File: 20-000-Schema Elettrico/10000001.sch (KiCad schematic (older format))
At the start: 1 part

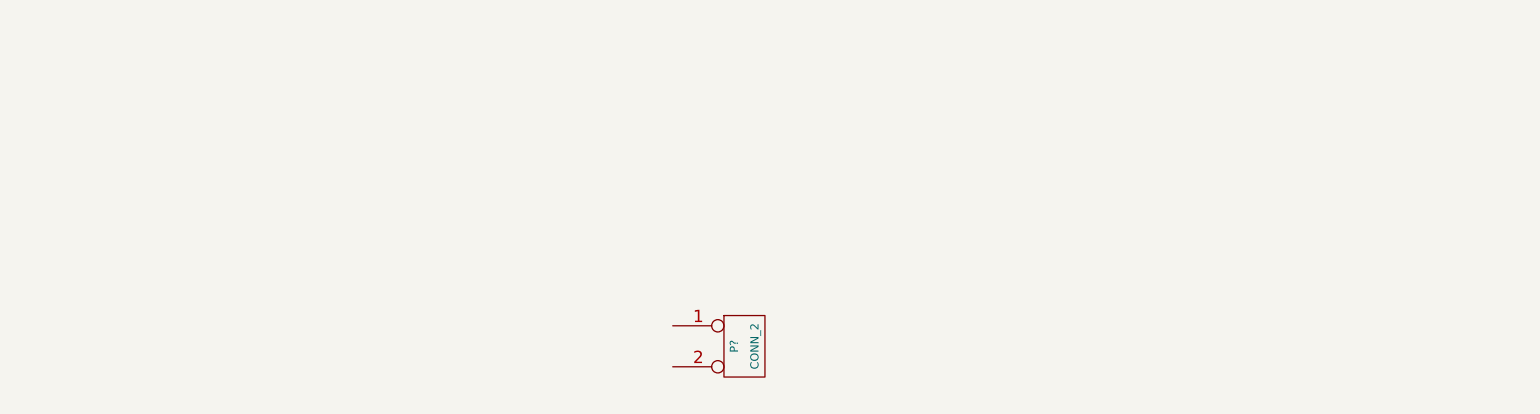
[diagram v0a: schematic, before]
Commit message: Aggiunti documenti di descrizione interfacce RS232, USB e distribuzione alimentazione... manca solo ADC!
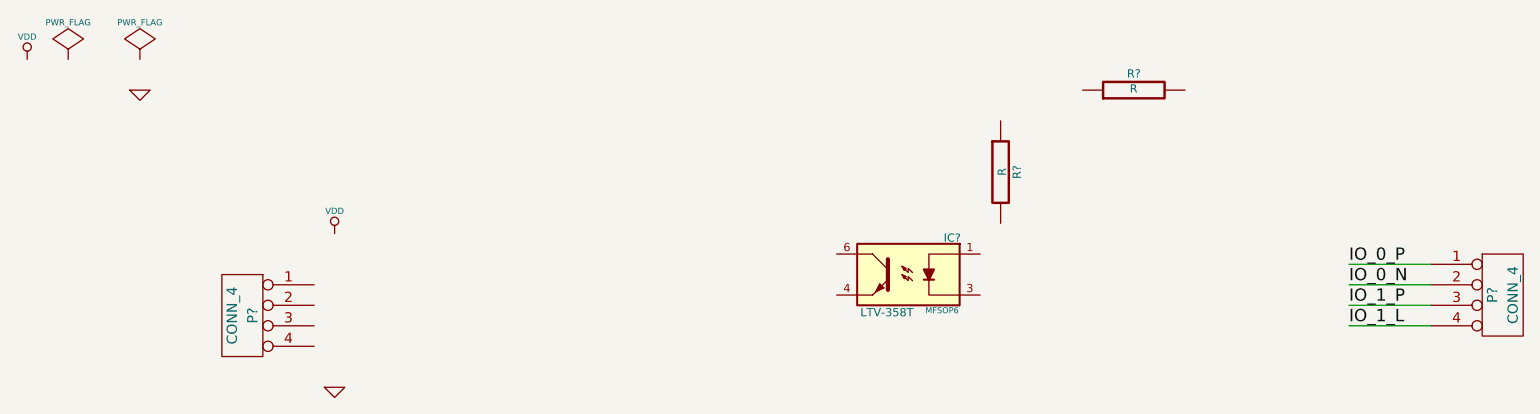
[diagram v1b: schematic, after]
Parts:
- removed P?: CONN_2, symbol CONN_2
- added IC?: LTV-358T, MFSOP6, symbol LTV-358T
- added P? (x2): CONN_4, symbol CONN_4
- added R? (x2): R, ~, symbol R
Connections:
- new net IO_0_N: P?.2 (P2)
- new net IO_0_P: P?.1 (P1)
- new net IO_1_L: P?.4 (P4)
- new net IO_1_P: P?.3 (P3)
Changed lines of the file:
@@
 Sheet 1 1
 Title "Input Output"
-Date "23 oct 2014"
+Date "2 nov 2014"
 Rev "0"
 Comp "OpenS"
@@
 $EndDescr
 $Comp
-L CONN_2 P?
-U 1 1 54497573
-P 5300 4500
-F 0 "P?" V 5250 4500 40  0000 C CNN
-F 1 "CONN_2" V 5350 4500 40  0000 C CNN
-F 2 "" H 5300 4500 60  0000 C CNN
-F 3 "" H 5300 4500 60  0000 C CNN
-	1    5300 4500
+L CONN_4 P?
+U 1 1 54560055
+P 2850 4350
+F 0 "P?" V 2800 4350 50  0000 C CNN
+F 1 "CONN_4" V 2900 4350 50  0000 C CNN
+F 2 "" H 2850 4350 60  0000 C CNN
+F 3 "" H 2850 4350 60  0000 C CNN
+	1    2850 4350
+	-1   0    0    -1
+$EndComp
+$Comp
+L CONN_4 P?
+U 1 1 545600A7
+P 9000 4250
+F 0 "P?" V 8950 4250 50  0000 C CNN
+F 1 "CONN_4" V 9050 4250 50  0000 C CNN
+F 2 "" H 9000 4250 60  0000 C CNN
+F 3 "" H 9000 4250 60  0000 C CNN
+	1    9000 4250
 	1    0    0    -1
 $EndComp
+$Comp
+L GND #PWR?
+U 1 1 545600E2
+P 3300 4700
+F 0 "#PWR?" H 3300 4700 30  0001 C CNN
+F 1 "GND" H 3300 4630 30  0001 C CNN
+F 2 "" H 3300 4700 60  0000 C CNN
+F 3 "" H 3300 4700 60  0000 C CNN
+	1    3300 4700
+	1    0    0    -1
+$EndComp
+$Comp
+L VDD #PWR?
+U 1 1 5456010A
+P 3300 3950
+F 0 "#PWR?" H 3300 4050 30  0001 C CNN
+F 1 "VDD" H 3300 4060 30  0000 C CNN
+F 2 "" H 3300 3950 60  0000 C CNN
+F 3 "" H 3300 3950 60  0000 C CNN
+	1    3300 3950
+	1    0    0    -1
+$EndComp
+$Comp
+L PWR_FLAG #FLG?
+U 1 1 54560122
+P 2000 3100
+F 0 "#FLG?" H 2000 3195 30  0001 C CNN
+F 1 "PWR_FLAG" H 2000 3280 30  0000 C CNN
+F 2 "" H 2000 3100 60  0000 C CNN
+F 3 "" H 2000 3100 60  0000 C CNN
+	1    2000 3100
+	1    0    0    -1
+$EndComp
+$Comp
+L PWR_FLAG #FLG?
+U 1 1 545601AD
+P 2350 3100
+F 0 "#FLG?" H 2350 3195 30  0001 C CNN
+F 1 "PWR_FLAG" H 2350 3280 30  0000 C CNN
+F 2 "" H 2350 3100 60  0000 C CNN
+F 3 "" H 2350 3100 60  0000 C CNN
+	1    2350 3100
+	1    0    0    -1
+$EndComp
+$Comp
+L VDD #PWR?
+U 1 1 545601B3
+P 1800 3100
+F 0 "#PWR?" H 1800 3200 30  0001 C CNN
+F 1 "VDD" H 1800 3210 30  0000 C CNN
+F 2 "" H 1800 3100 60  0000 C CNN
+F 3 "" H 1800 3100 60  0000 C CNN
+	1    1800 3100
+	1    0    0    -1
+$EndComp
+$Comp
+L GND #PWR?
+U 1 1 545601B9
+P 2350 3250
+F 0 "#PWR?" H 2350 3250 30  0001 C CNN
+F 1 "GND" H 2350 3180 30  0001 C CNN
+F 2 "" H 2350 3250 60  0000 C CNN
+F 3 "" H 2350 3250 60  0000 C CNN
+	1    2350 3250
+	1    0    0    -1
+$EndComp
+$Comp
+L LTV-358T IC?
+U 1 1 5456058E
+P 6100 4150
+F 0 "IC?" H 5886 4329 40  0000 C CNN
+F 1 "LTV-358T" H 6205 3965 40  0000 C CNN
+F 2 "MFSOP6" H 5936 3975 29  0000 C CNN
+F 3 "" H 6100 4150 60  0000 C CNN
+	1    6100 4150
+	-1   0    0    -1
+$EndComp
+Wire Wire Line
+	8650 4100 8250 4100
+Wire Wire Line
+	8650 4200 8250 4200
+Wire Wire Line
+	8650 4300 8250 4300
+Wire Wire Line
+	8650 4400 8250 4400
+Text Label 8250 4100 0    60   ~ 0
+IO_0_P
+Text Label 8250 4200 0    60   ~ 0
+IO_0_N
+Text Label 8250 4300 0    60   ~ 0
+IO_1_P
+Text Label 8250 4400 0    60   ~ 0
+IO_1_L
+$Comp
+L R R?
+U 1 1 5456065C
+P 6550 3650
+F 0 "R?" V 6630 3650 40  0000 C CNN
+F 1 "R" V 6557 3651 40  0000 C CNN
+F 2 "~" V 6480 3650 30  0000 C CNN
+F 3 "~" H 6550 3650 30  0000 C CNN
+	1    6550 3650
+	1    0    0    -1
+$EndComp
+$Comp
+L R R?
+U 1 1 54560669
+P 7200 3250
+F 0 "R?" V 7280 3250 40  0000 C CNN
+F 1 "R" V 7207 3251 40  0000 C CNN
+F 2 "~" V 7130 3250 30  0000 C CNN
+F 3 "~" H 7200 3250 30  0000 C CNN
+	1    7200 3250
+	0    -1   -1   0
+$EndComp
 $EndSCHEMATC

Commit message: Aggiornato schematico modulo ingressi
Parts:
- removed R?: R, ~, symbol R
- added D? (x2): ZENERSMALL, symbol ZENERSMALL
- added IC?: LTV-358T, MFSOP6, symbol LTV-358T
- added P? (x6): CONN_4, symbol CONN_4
- added R? (x5): 10000, ~, symbol R
- added R?: 1000, ~, symbol R
- added R? (x4): 2400, ~, symbol R
- added R? (x2): 100, ~, symbol R
- added R? (x6): 0, ~, symbol R
- added U?: PCF8574, symbol PCF8574
- R?: value R -> 1000
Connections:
- net labels added: I2C_INT, I2C_SCL, I2C_SDA, IO_0_CMD, IO_1_CMD, IO_1_N, IO_2_CMD, IO_3_CMD, IO_4_CMD, IO_5_CMD, IO_6_CMD, IO_7_CMD
- wire segments 4 -> 115
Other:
- moved on the sheet: IC?, P?, R?

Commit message: Aggiornato schema
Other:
- note added: "Connettori di rimando laterali"
- note added: "Ingresso I2C"
- note added: "Protezioni lato utente"
- note added: "Selettori connessioni di rimando"
- moved on the sheet: P?, R?
